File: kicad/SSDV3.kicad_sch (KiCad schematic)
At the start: 8 parts, among them J7 SolderPad_1x02, J8 SolderPad_1x03

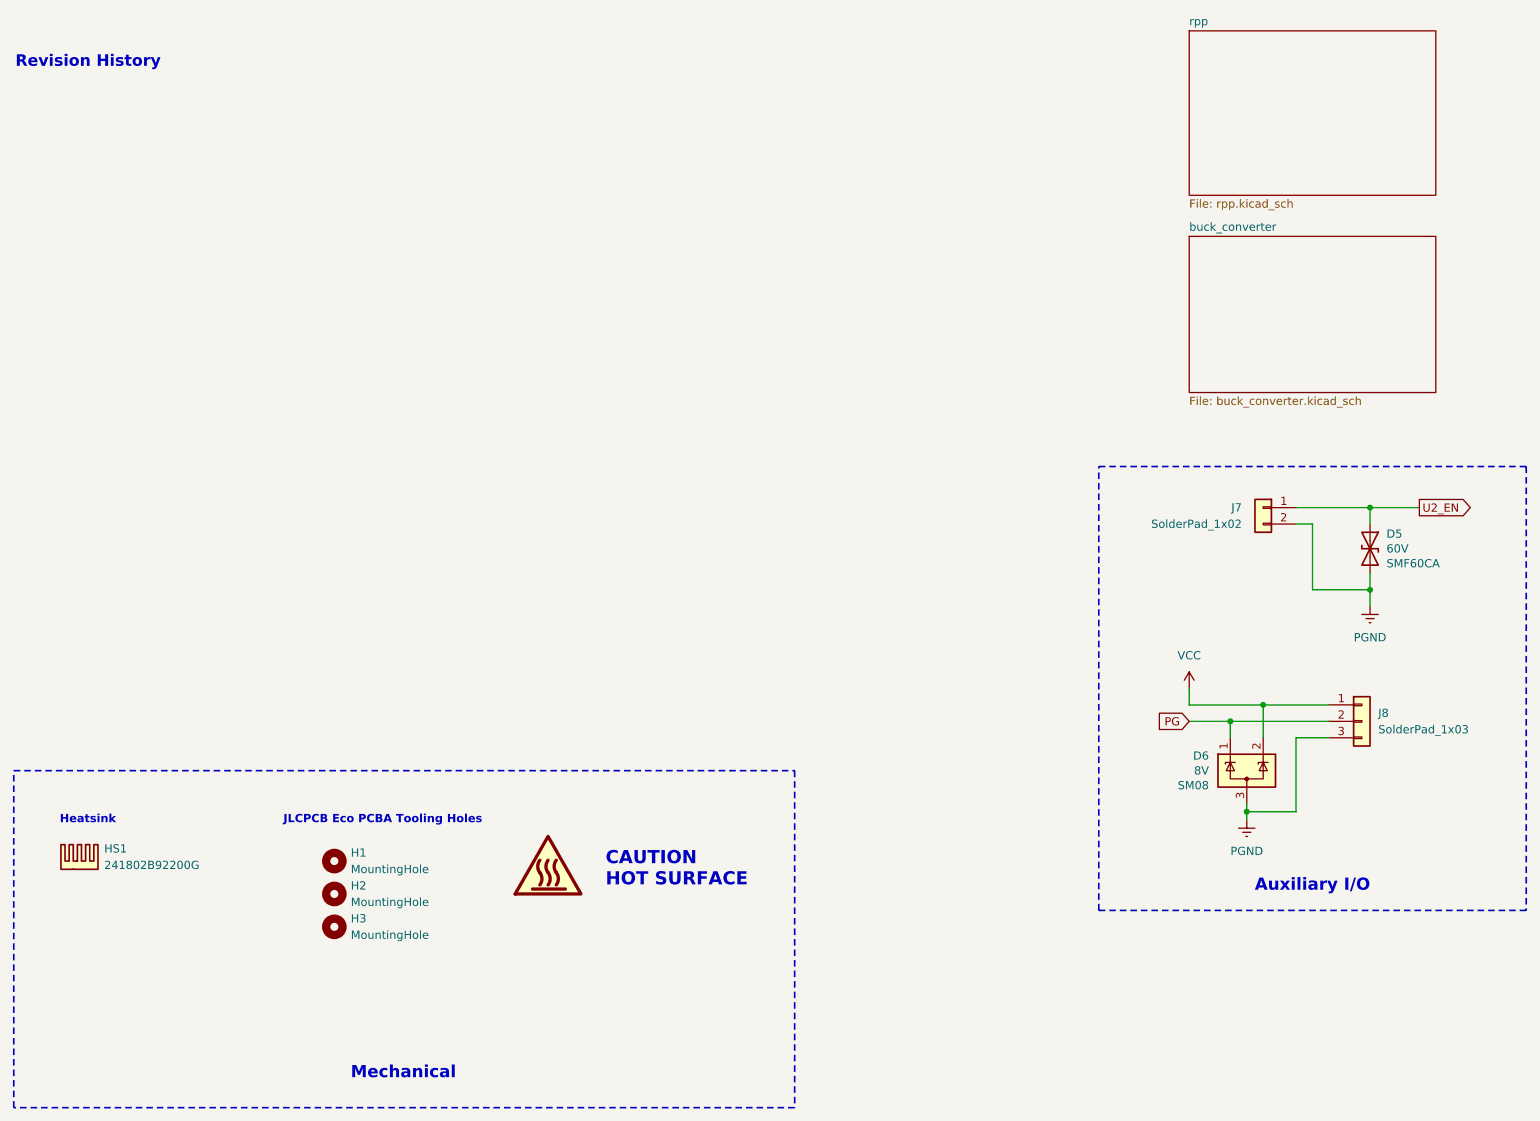
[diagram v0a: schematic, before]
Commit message: Created redesign for revD to reduce thermal stress
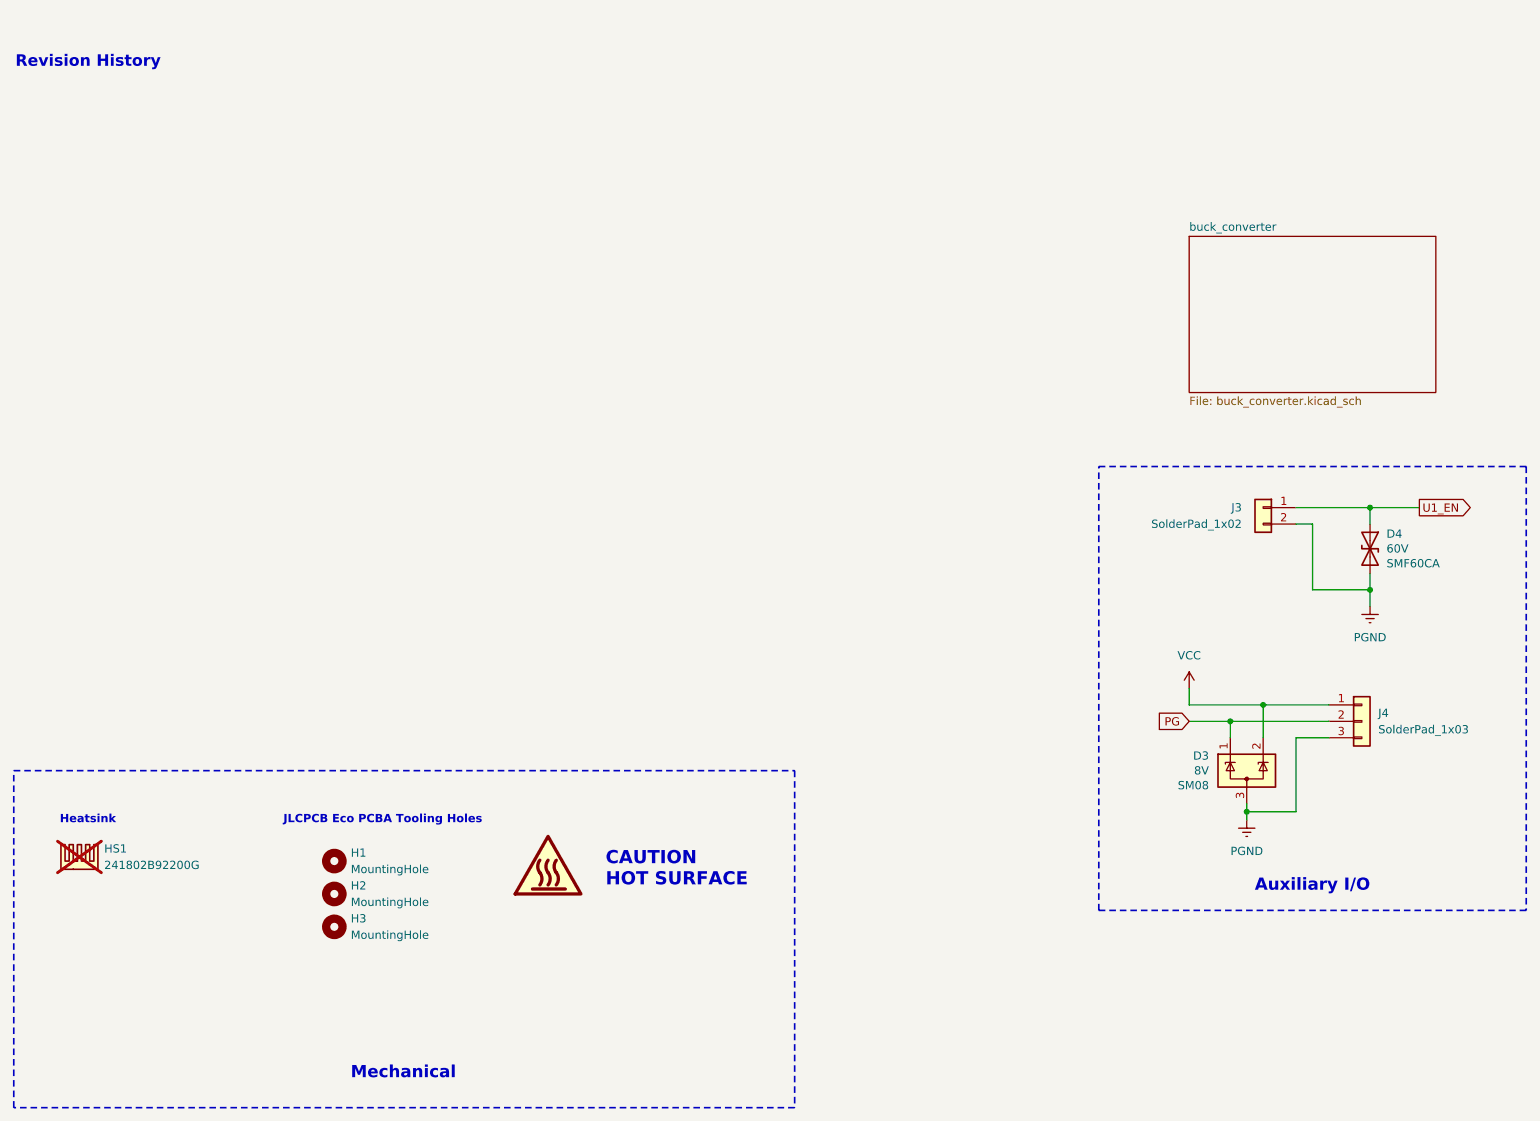
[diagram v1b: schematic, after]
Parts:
- HS1: now not fitted
- renumbered D6 to D3, D5 to D4, J7 to J3, J8 to J4
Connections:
- net U2_EN renamed U1_EN
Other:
- removed sheet rpp
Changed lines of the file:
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@@
 		)
 	)
-	(global_label "U2_EN"
+	(global_label "U1_EN"
 		(shape output)
 		(at 242.57 100.33 0)
@@
 		(dnp no)
 		(fields_autoplaced yes)
-		(property "Reference" "#PWR030"
+		(property "Reference" "#PWR018"
 			(at 207.01 132.08 0)
 			(effects
@@
 			(project "2025_SSDP3A2"
 				(path "/ea689c3b-fea3-4fc0-9d65-1fb672b240d8"
-					(reference "#PWR030")
+					(reference "#PWR018")
 					(unit 1)
 				)
@@
 		(on_board yes)
 		(dnp no)
-		(property "Reference" "#PWR027"
+		(property "Reference" "#PWR020"
 			(at 234.95 121.92 0)
 			(effects
@@
 			(project "2025_SSDP3A2"
 				(path "/ea689c3b-fea3-4fc0-9d65-1fb672b240d8"
-					(reference "#PWR027")
+					(reference "#PWR020")
 					(unit 1)
 				)
@@
 		(on_board yes)
 		(dnp no)
-		(property "Reference" "#PWR025"
+		(property "Reference" "#PWR019"
 			(at 215.9 154.94 0)
 			(effects
@@
 			(project "2025_SSDP3A2"
 				(path "/ea689c3b-fea3-4fc0-9d65-1fb672b240d8"
-					(reference "#PWR025")
+					(reference "#PWR019")
 					(unit 1)
 				)
@@
 		(dnp no)
 		(fields_autoplaced yes)
-		(property "Reference" "J8"
+		(property "Reference" "J4"
 			(at 236.22 132.08 0)
 			(effects
@@
 			(project ""
 				(path "/ea689c3b-fea3-4fc0-9d65-1fb672b240d8"
-					(reference "J8")
+					(reference "J4")
 					(unit 1)
 				)
@@
 		(on_board yes)
 		(dnp no)
-		(property "Reference" "D5"
+		(property "Reference" "D4"
 			(at 237.49 104.394 90)
 			(effects
@@
 			(project ""
 				(path "/ea689c3b-fea3-4fc0-9d65-1fb672b240d8"
-					(reference "D5")
+					(reference "D4")
 					(unit 1)
 				)
@@
 		(on_board yes)
 		(dnp no)
-		(property "Reference" "D6"
+		(property "Reference" "D3"
 			(at 210.058 138.684 0)
 			(effects
@@
 			(project ""
 				(path "/ea689c3b-fea3-4fc0-9d65-1fb672b240d8"
-					(reference "D6")
+					(reference "D3")
 					(unit 1)
 				)
@@
 		(exclude_from_sim yes)
 		(in_bom no)
-		(on_board yes)
-		(dnp no)
+		(on_board no)
+		(dnp yes)
 		(fields_autoplaced yes)
 		(property "Reference" "HS1"
@@
 		(on_board yes)
 		(dnp no)
-		(property "Reference" "J7"
+		(property "Reference" "J3"
 			(at 215.138 100.33 0)
 			(effects
@@
 			(project ""
 				(path "/ea689c3b-fea3-4fc0-9d65-1fb672b240d8"
-					(reference "J7")
+					(reference "J3")
 					(unit 1)
 				)
 			)
-		)
-	)
-	(sheet
-		(at 207.01 26.67)
-		(size 38.1 25.4)
-		(exclude_from_sim no)
-		(in_bom yes)
-		(on_board yes)
-		(dnp no)
-		(fields_autoplaced yes)
-		(stroke
-			(width 0.1524)
-			(type solid)
-		)
-		(fill
-			(color 0 0 0 0.0000)
-		)
-		(property "Sheetname" "rpp"
-			(at 207.01 25.9584 0)
-			(effects
-				(font
-					(size 1.27 1.27)
-				)
-				(justify left bottom)
-			)
-		)
-		(property "Sheetfile" "rpp.kicad_sch"
-			(at 207.01 52.6546 0)
-			(effects
-				(font
-					(size 1.27 1.27)
-				)
-				(justify left top)
-			)
-		)
-		(instances
-			(project "SSDV3"
-				(path "/ea689c3b-fea3-4fc0-9d65-1fb672b240d8"
-					(page "2")
-				)
-			)
